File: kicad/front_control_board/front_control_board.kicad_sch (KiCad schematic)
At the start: 66 parts, among them J1 MAIN_BOARD, J2 DISPLAY, J3 PROG, J4 I2C, J5 AUX, J6 LED_OUT, Q1 AO3401A, SW1 PEC11R-4215K-S0024, SW2 BTN1, SW3 BTN4, SW4 BTN2, SW5 BTN3, U1 ESP32-WROOM-32UE, U2 TCA9534

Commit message: fix invalid bom number
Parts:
- BZ1: LCSC C3812136 -> C409834
- D1, D10, D3, D4, D5, D6, D7, D8, D9: LCSC C114586 -> C2761795
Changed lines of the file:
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@@
 	(title_block
 		(title "SW32 - Front Control Board")
-		(date "2024-05-23")
+		(date "2024-05-26")
 		(rev "1")
 		(company "saawsm")
@@
 			)
 		)
-		(property "Datasheet" "https://www.lcsc.com/datasheet/lcsc_datasheet_2006151006_Worldsemi-WS2812B-B-W_C114586.pdf"
+		(property "Datasheet" "https://www.lcsc.com/datasheet/lcsc_datasheet_2106062036_Worldsemi-WS2812B-B-T_C2761795.pdf"
 			(at 187.96 40.005 0)
 			(effects
@@
 			)
 		)
-		(property "LCSC" "C114586"
+		(property "LCSC" "C2761795"
 			(at 185.42 30.48 0)
 			(effects
@@
 			)
 		)
-		(property "Datasheet" "https://www.lcsc.com/datasheet/lcsc_datasheet_2006151006_Worldsemi-WS2812B-B-W_C114586.pdf"
+		(property "Datasheet" "https://www.lcsc.com/datasheet/lcsc_datasheet_2106062036_Worldsemi-WS2812B-B-T_C2761795.pdf"
 			(at 246.38 40.005 0)
 			(effects
@@
 			)
 		)
-		(property "LCSC" "C114586"
+		(property "LCSC" "C2761795"
 			(at 243.84 30.48 0)
 			(effects
@@
 			)
 		)
-		(property "Datasheet" "https://www.lcsc.com/datasheet/lcsc_datasheet_2006151006_Worldsemi-WS2812B-B-W_C114586.pdf"
+		(property "Datasheet" "https://www.lcsc.com/datasheet/lcsc_datasheet_2106062036_Worldsemi-WS2812B-B-T_C2761795.pdf"
 			(at 102.87 40.005 0)
 			(effects
@@
 			)
 		)
-		(property "LCSC" "C114586"
+		(property "LCSC" "C2761795"
 			(at 100.33 30.48 0)
 			(effects
@@
 			)
 		)
-		(property "Datasheet" "https://www.lcsc.com/datasheet/lcsc_datasheet_2006151006_Worldsemi-WS2812B-B-W_C114586.pdf"
+		(property "Datasheet" "https://www.lcsc.com/datasheet/lcsc_datasheet_2106062036_Worldsemi-WS2812B-B-T_C2761795.pdf"
 			(at 213.36 40.005 0)
 			(effects
@@
 			)
 		)
-		(property "LCSC" "C114586"
+		(property "LCSC" "C2761795"
 			(at 210.82 30.48 0)
 			(effects
@@
 			)
 		)
-		(property "Datasheet" "https://www.lcsc.com/datasheet/lcsc_datasheet_2006151006_Worldsemi-WS2812B-B-W_C114586.pdf"
+		(property "Datasheet" "https://www.lcsc.com/datasheet/lcsc_datasheet_2106062036_Worldsemi-WS2812B-B-T_C2761795.pdf"
 			(at 262.89 40.005 0)
 			(effects
@@
 			)
 		)
-		(property "LCSC" "C114586"
+		(property "LCSC" "C2761795"
 			(at 260.35 30.48 0)
 			(effects
@@
 			)
 		)
-		(property "Datasheet" "https://www.lcsc.com/datasheet/lcsc_datasheet_2006151006_Worldsemi-WS2812B-B-W_C114586.pdf"
+		(property "Datasheet" "https://www.lcsc.com/datasheet/lcsc_datasheet_2106062036_Worldsemi-WS2812B-B-T_C2761795.pdf"
 			(at 147.32 40.005 0)
 			(effects
@@
 			)
 		)
-		(property "LCSC" "C114586"
+		(property "LCSC" "C2761795"
 			(at 144.78 30.48 0)
 			(effects
@@
 			)
 		)
-		(property "Datasheet" "https://www.lcsc.com/datasheet/lcsc_datasheet_2006151006_Worldsemi-WS2812B-B-W_C114586.pdf"
+		(property "Datasheet" "https://www.lcsc.com/datasheet/lcsc_datasheet_2106062036_Worldsemi-WS2812B-B-T_C2761795.pdf"
 			(at 130.81 40.005 0)
 			(effects
@@
 			)
 		)
-		(property "LCSC" "C114586"
+		(property "LCSC" "C2761795"
 			(at 128.27 30.48 0)
 			(effects
@@
 			)
 		)
-		(property "Datasheet" "https://www.lcsc.com/datasheet/lcsc_datasheet_2006151006_Worldsemi-WS2812B-B-W_C114586.pdf"
+		(property "Datasheet" "https://www.lcsc.com/datasheet/lcsc_datasheet_2106062036_Worldsemi-WS2812B-B-T_C2761795.pdf"
 			(at 229.87 40.005 0)
 			(effects
@@
 			)
 		)
-		(property "LCSC" "C114586"
+		(property "LCSC" "C2761795"
 			(at 227.33 30.48 0)
 			(effects
@@
 			)
 		)
-		(property "LCSC" "C3812136"
+		(property "LCSC" "C409834"
 			(at 59.69 90.17 0)
 			(effects
@@
 			)
 		)
-		(property "Datasheet" "https://www.lcsc.com/datasheet/lcsc_datasheet_2006151006_Worldsemi-WS2812B-B-W_C114586.pdf"
+		(property "Datasheet" "https://www.lcsc.com/datasheet/lcsc_datasheet_2106062036_Worldsemi-WS2812B-B-T_C2761795.pdf"
 			(at 171.45 40.005 0)
 			(effects
@@
 			)
 		)
-		(property "LCSC" "C114586"
+		(property "LCSC" "C2761795"
 			(at 168.91 30.48 0)
 			(effects

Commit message: update LED part number
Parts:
- D1, D10, D3, D4, D5, D6, D7, D8, D9: LCSC C2761795 -> C2843785
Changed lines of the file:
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@@
 			)
 		)
-		(property "LCSC" "C2761795"
+		(property "LCSC" "C2843785"
 			(at 185.42 30.48 0)
 			(effects
@@
 			)
 		)
-		(property "LCSC" "C2761795"
+		(property "LCSC" "C2843785"
 			(at 243.84 30.48 0)
 			(effects
@@
 			)
 		)
-		(property "LCSC" "C2761795"
+		(property "LCSC" "C2843785"
 			(at 100.33 30.48 0)
 			(effects
@@
 			)
 		)
-		(property "LCSC" "C2761795"
+		(property "LCSC" "C2843785"
 			(at 210.82 30.48 0)
 			(effects
@@
 			)
 		)
-		(property "LCSC" "C2761795"
+		(property "LCSC" "C2843785"
 			(at 260.35 30.48 0)
 			(effects
@@
 			)
 		)
-		(property "LCSC" "C2761795"
+		(property "LCSC" "C2843785"
 			(at 144.78 30.48 0)
 			(effects
@@
 			)
 		)
-		(property "LCSC" "C2761795"
+		(property "LCSC" "C2843785"
 			(at 128.27 30.48 0)
 			(effects
@@
 			)
 		)
-		(property "LCSC" "C2761795"
+		(property "LCSC" "C2843785"
 			(at 227.33 30.48 0)
 			(effects
@@
 			)
 		)
-		(property "LCSC" "C2761795"
+		(property "LCSC" "C2843785"
 			(at 168.91 30.48 0)
 			(effects

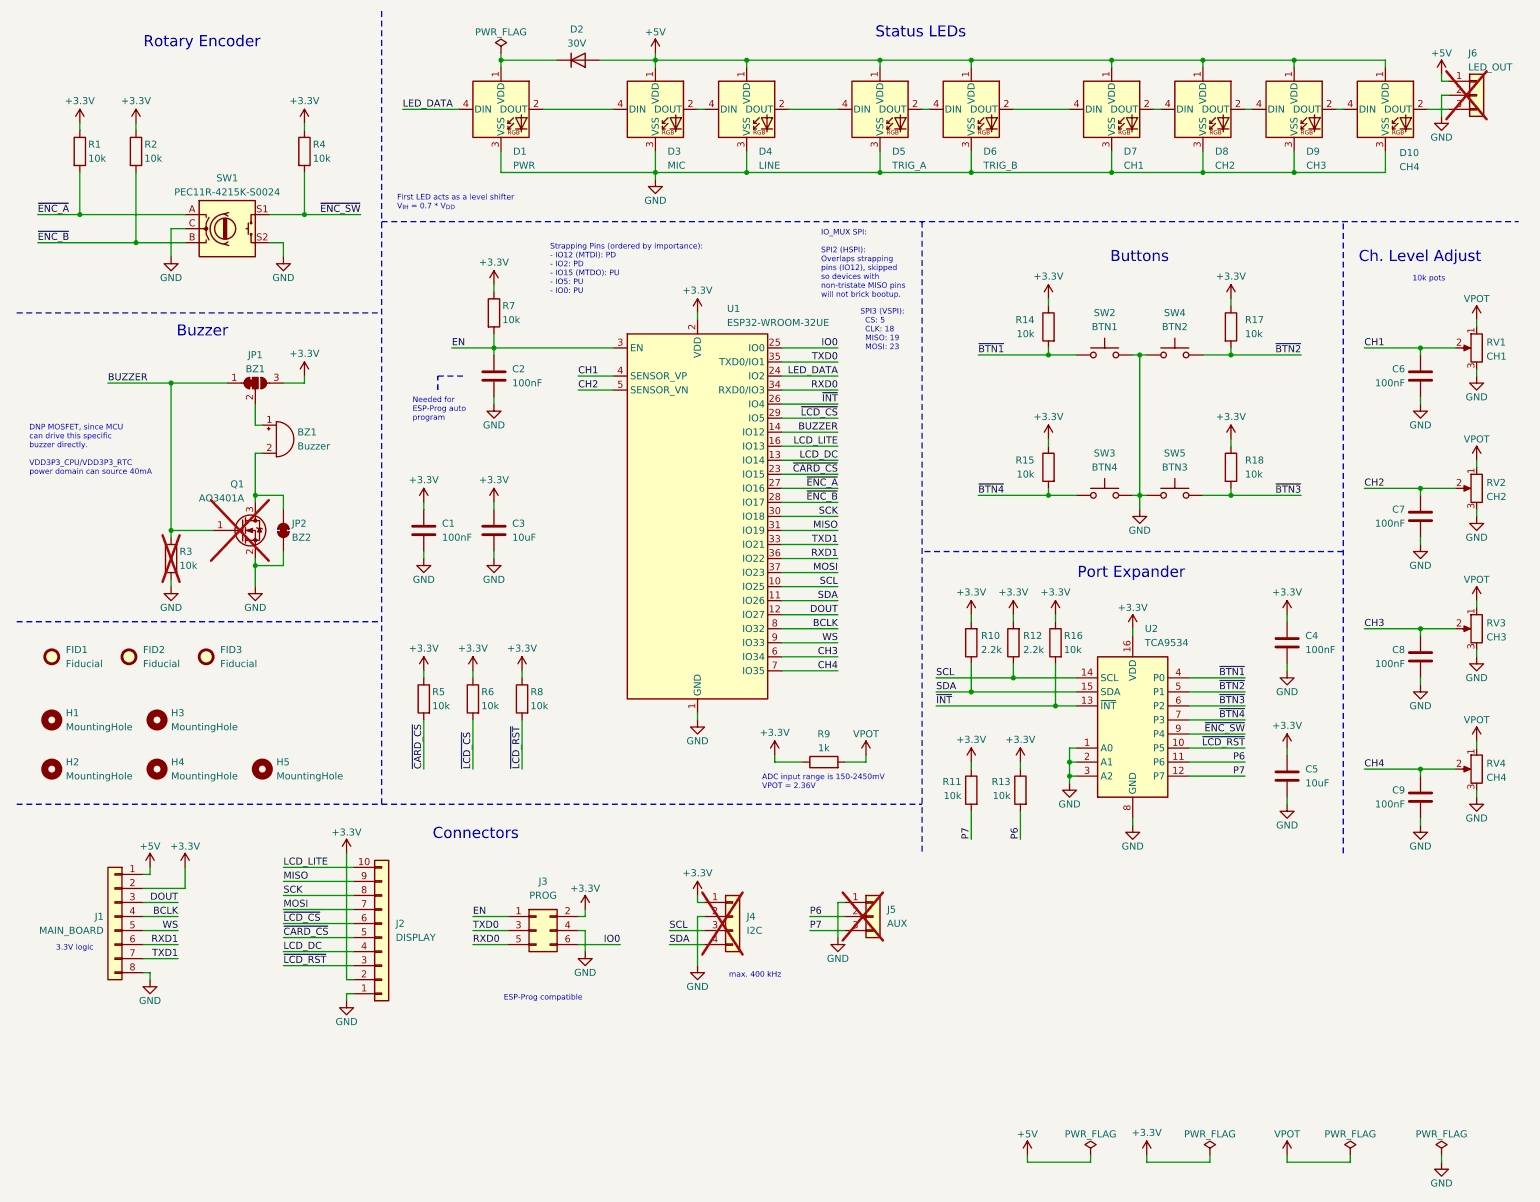
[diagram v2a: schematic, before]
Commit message: remove port expander
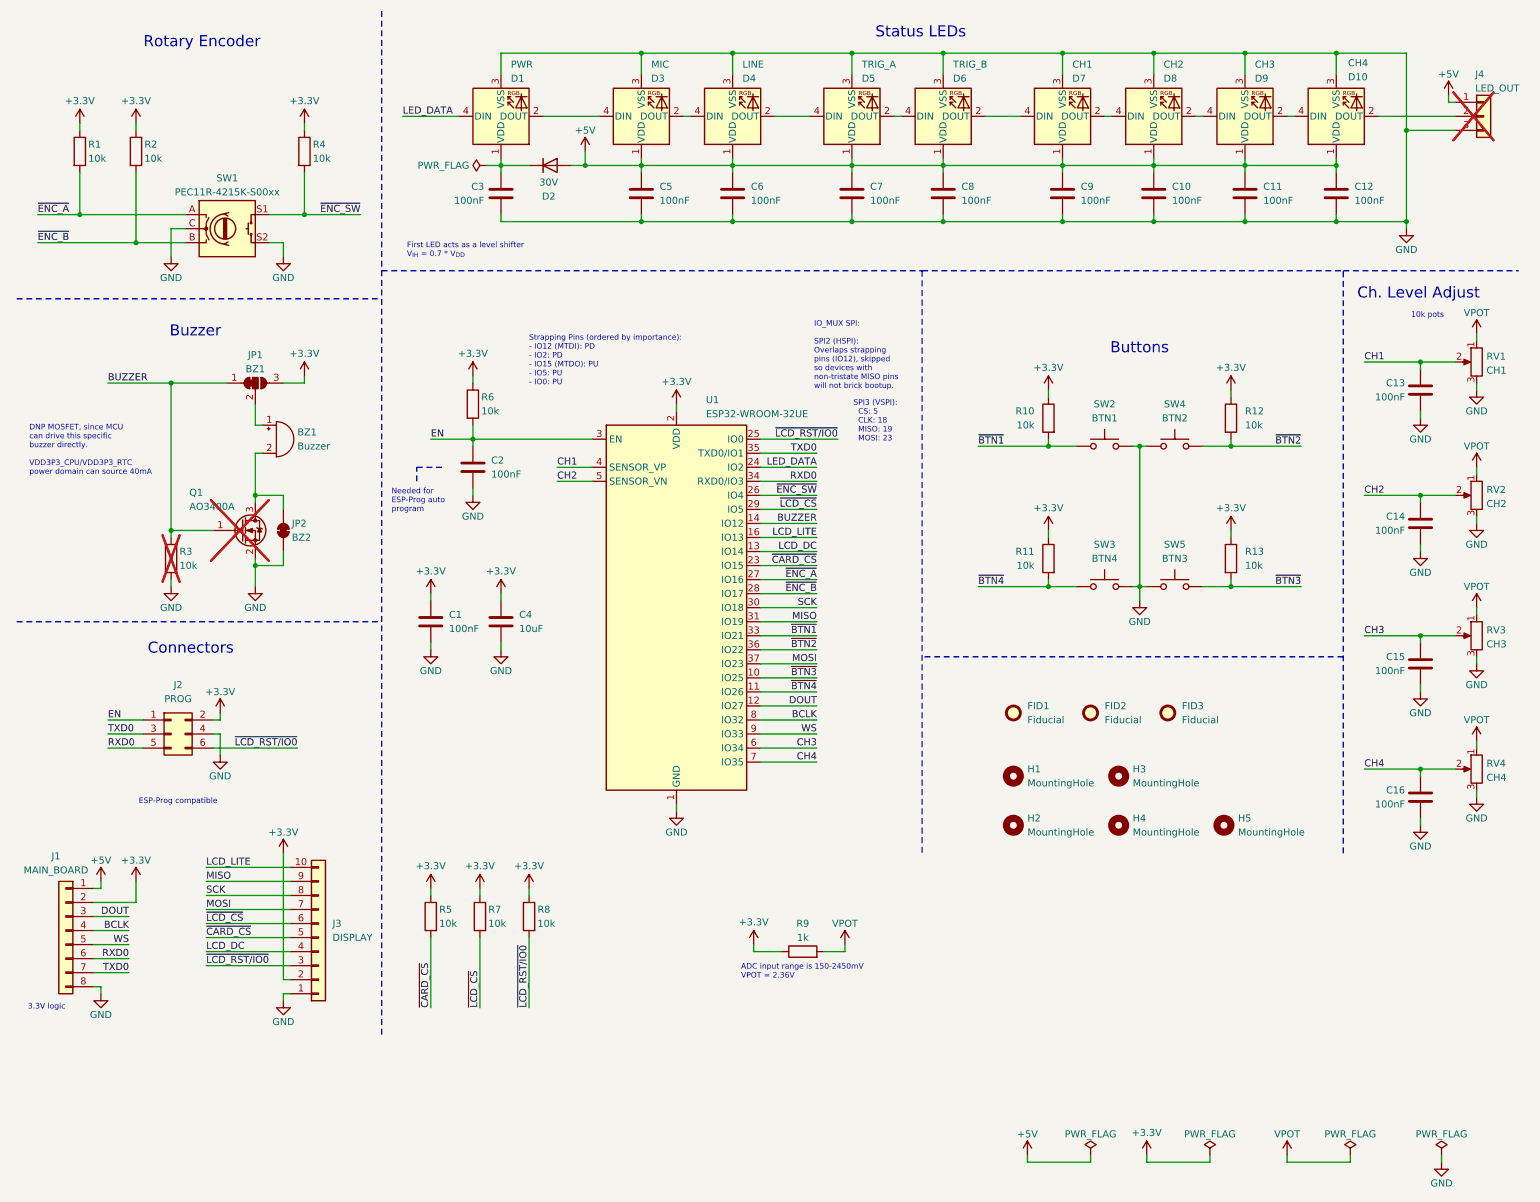
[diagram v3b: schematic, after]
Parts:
- removed C4: 100nF, Capacitor_SMD:C_0603_1608Metric, symbol Device:C
- removed J4: I2C, Connector_PinHeader_2.54mm:PinHeader_1x04_P2.54mm_Vertical, symbol Connector_Generic:Conn_01x04
- removed J5: AUX, Connector_PinHeader_2.54mm:PinHeader_1x03_P2.54mm_Vertical, symbol Connector_Generic:Conn_01x03
- removed R10, R12: 2.2k, Resistor_SMD:R_0603_1608Metric, symbol Device:R
- removed R11, R13, R16: 10k, Resistor_SMD:R_0603_1608Metric, symbol Device:R
- removed U2: TCA9534, Package_SO:TSSOP-16_4.4x5mm_P0.65mm, symbol Interface_Expansion:TCA9534
- added C10, C11, C12, C3, C6, C7, C8, C9: 100nF, Capacitor_SMD:C_0603_1608Metric, symbol Device:C
- C5: value 10uF -> 100nF; LCSC C96446 -> C14663
- Q1: value AO3401A -> AO3400A; LCSC C15127 -> C20917
- SW1: value PEC11R-4215K-S0024 -> PEC11R-4215K-S00xx
- renumbered C6 to C13, C7 to C14, C8 to C15, C9 to C16, C3 to C4, J3 to J2, J2 to J3, J6 to J4, R14 to R10, R15 to R11, R17 to R12, R18 to R13, R7 to R6, R6 to R7
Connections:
- net SCL is gone; now on net ~{BTN3}: U1.10 (IO25)
- net SDA is gone; now on net ~{BTN4}: U1.11 (IO26)
- net ~{INT} is gone; now on net ~{ENC_SW}: U1.26 (IO4)
- net ~{LCD_RST} is gone; now on net ~{LCD_RST/IO0}: J3.3 (Pin_3), R8.2
- net +3.3V: no longer C5.1
- net +5V: now also C5.1, C10.1, C11.1, C12.1, C6.1, C7.1, C8.1, C9.1
- net GND: now also J4.3 (Pin_3), C10.2, C11.2, C12.2, C3.2, C6.2, C7.2, C8.2, C9.2; no longer J4.2 (Pin_2)
- net RXD0: now also J1.6 (Pin_6)
- net TXD0: now also J1.7 (Pin_7)
- net ~{BTN1}: now also U1.33 (IO21)
- net ~{BTN2}: now also U1.36 (IO22)
- net at D1.1 (VDD), D2.1 (K): now also C3.1
- net at D10.2 (DOUT): now also J4.2 (Pin_2); no longer J4.3 (Pin_3)
- net IO0 renamed ~{LCD_RST/IO0}
- removed net RXD1: J1.6 (Pin_6), U1.36 (IO22)
- removed net TXD1: J1.7 (Pin_7), U1.33 (IO21)
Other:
- note removed: "Port Expander"
- note removed: "max. 400 kHz"
- moved on the sheet: C1, C13, C14, C15, C2, C4, D1, D10, D2, D3, D4, D5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

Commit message: add status led for USB connector
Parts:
- added C5: 100nF, Capacitor_SMD:C_0603_1608Metric, symbol Device:C
- added D3: USB, LED_SMD:LED_WS2812B_PLCC4_5.0x5.0mm_P3.2mm, symbol LED:WS2812B
- added H5: MountingHole, MountingHole:MountingHole_2.2mm_M2, symbol Mechanical:MountingHole
- renumbered C9 to C10, C10 to C11, C11 to C12, C12 to C13, C13 to C14, C14 to C15, C15 to C16, C16 to C17, C5 to C6, C6 to C7, C7 to C8, C8 to C9, D9 to D10, D10 to D11, D3 to D4, D4 to D5, D5 to D6, D6 to D7, D7 to D8, D8 to D9, H5 to H6
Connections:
- net +5V: now also C5.1, D3.1 (VDD)
- net GND: now also C5.2, D3.3 (VSS)
- net at D4.4 (DIN): now also D3.2 (DOUT); no longer D1.2 (DOUT)
- new net: D1.2 (DOUT), D3.4 (DIN)
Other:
- moved on the sheet: C10, C11, C12, C13, C3, C6, C7, C8, C9, D1, D10, D11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

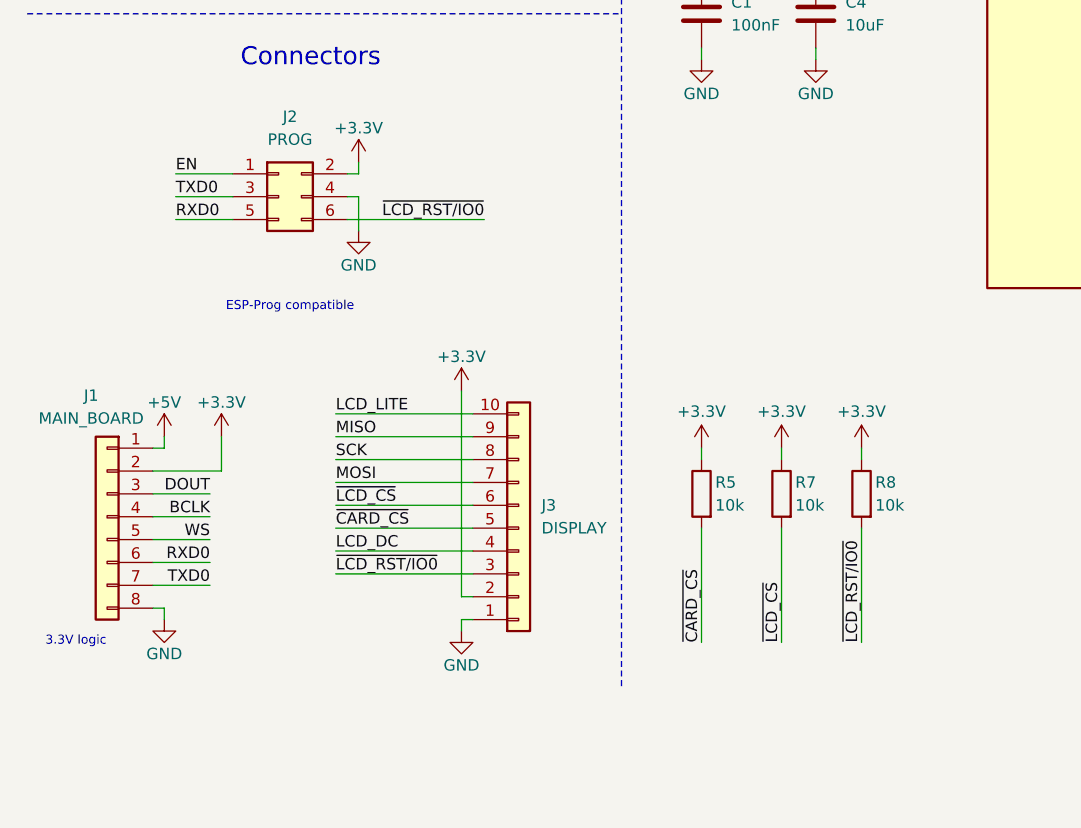
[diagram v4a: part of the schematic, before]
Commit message: use 2x4 IDC connector
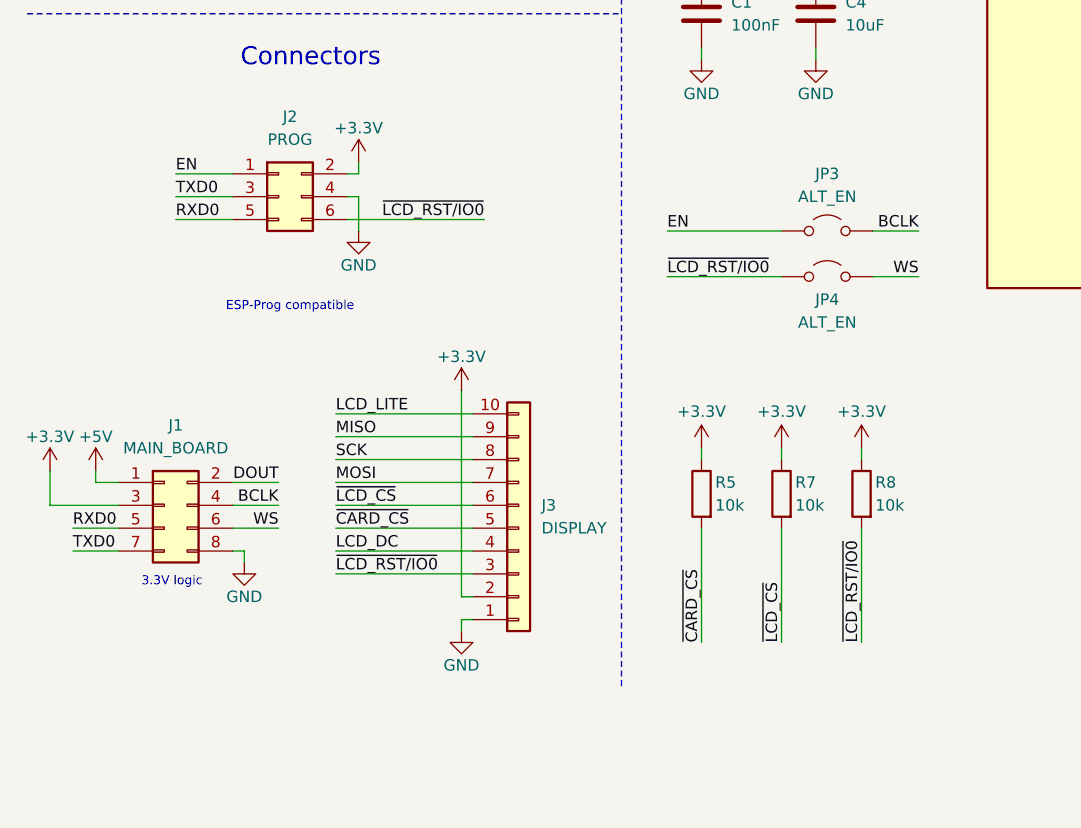
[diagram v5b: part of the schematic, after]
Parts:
- added JP3, JP4: ALT_EN, symbol Jumper:Jumper_2_Open
- J1: footprint Connector_JST:JST_XH_B8B-XH-A_1x08_P2.50mm_Vertical -> Connector_IDC:IDC-Header_2x04_P2.54mm_Vertical; symbol Connector_Generic:Conn_01x08 -> Connector_Generic:Conn_02x04_Odd_Even; LCSC C7429638 -> C5372864
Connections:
- net +3.3V: now also J1.3 (Pin_3); no longer J1.2 (Pin_2)
- net BCLK: now also JP3.2 (B)
- net DOUT: now also J1.2 (Pin_2); no longer J1.3 (Pin_3)
- net EN: now also JP3.1 (A)
- net RXD0: now also J1.5 (Pin_5); no longer J1.6 (Pin_6)
- net WS: now also J1.6 (Pin_6), JP4.2 (B); no longer J1.5 (Pin_5)
- net ~{LCD_RST/IO0}: now also JP4.1 (A)
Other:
- moved on the sheet: J1
